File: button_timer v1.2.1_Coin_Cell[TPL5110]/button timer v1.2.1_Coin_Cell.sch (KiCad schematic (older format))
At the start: 24 parts, among them J1 Conn_01x05_Female, SW1 SW_Push, SW2 SW_Push, U1 TPS61097A, U3 TPL5111, X1 ESP-12E

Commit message: :rocket: :full_moon_with_face:
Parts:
- removed U3: TPL5111, handsolder:SOT-23-6handsoldering, symbol button-timer-v1.2.1_Coin_Cell-rescue:TPL5111-Timer-button-timer-rescue-button-t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
- added Q1: TSM2323, Package_TO_SOT_SMD:SOT-23, symbol Transistor_FET:TSM2301ACX
- added U2: TPL5110, Package_TO_SOT_SMD:SOT-23-6, symbol Timer:TPL5110
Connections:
- net GND: now also U2.2 (GND), U2.6 (EN/ONE_SHOT)
- net GPIO4: now also U2.4 (DONE)
- net at BT1.1 (+), C1.2, C5.2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: now also Q1.2 (S), U2.1 (VDD); no longer L1.1, U1.1 (VIN)
- net at R6.2, R8.2, SW1.2: now also U2.3 (DELAY/M_DRV)
- net at R7.1: now also U1.3 (EN)
- net at R7.2: now also L1.1, U1.1 (VIN), Q1.3 (D); no longer U1.3 (EN)
- new net: Q1.1 (G), U2.5 (DRV)
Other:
- moved on the sheet: C3, L1, R7, U1
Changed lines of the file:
@@
 Wire Wire Line
 	1300 5750 1300 5650
-$Comp
-L button-timer-v1.2.1_Coin_Cell-rescue:TPL5111-Timer-button-timer-rescue-button-timer-v1.2-rescue-button-timer-v1.2-rescue U3
-U 1 1 6031B6A7
-P 2250 5650
-F 0 "U3" H 2200 6331 50  0000 C CNN
-F 1 "TPL5111" H 2200 6240 50  0000 C CNN
-F 2 "handsolder:SOT-23-6handsoldering" H 2250 5650 50  0001 C CNN
-F 3 "http://www.ti.com/lit/ds/symlink/tpl5111.pdf" H 600 5800 50  0001 C CNN
-	1    2250 5650
-	1    0    0    -1
-$EndComp
 Text Label 2250 6050 3    50   ~ 0
 GND
@@
 Wire Wire Line
 	2650 4150 2700 4150
-Wire Wire Line
-	2750 5550 3050 5550
 Text Label 1650 5550 2    50   ~ 0
 GND
@@
 	2250 4150 2550 4150
 Wire Wire Line
-	2900 4400 2900 4100
+	4050 4700 4050 4400
 Wire Wire Line
 	2200 4150 2200 4350
@@
 L button-timer-v1.2.1_Coin_Cell-rescue:R-Device-button-timer-rescue-button-timer-v1.2-rescue-button-timer-v1.2-rescue R7
 U 1 1 602F7A06
-P 3200 5550
-F 0 "R7" H 3270 5596 50  0000 L CNN
-F 1 "10k" H 3270 5505 50  0000 L CNN
-F 2 "handsolder:R_0805_2012handsoldermod" V 3130 5550 50  0001 C CNN
-F 3 "~" H 3200 5550 50  0001 C CNN
-	1    3200 5550
-	0    -1   -1   0
-$EndComp
-Wire Wire Line
-	2700 4100 2900 4100
+P 4500 5700
+F 0 "R7" H 4570 5746 50  0000 L CNN
+F 1 "10k" H 4570 5655 50  0000 L CNN
+F 2 "handsolder:R_0805_2012handsoldermod" V 4430 5700 50  0001 C CNN
+F 3 "~" H 4500 5700 50  0001 C CNN
+	1    4500 5700
+	-1   0    0    1
+$EndComp
 Text Label 1500 5950 3    50   ~ 0
 GND
@@
 Wire Wire Line
 	1300 5650 1200 5650
-Connection ~ 2900 4100
-Wire Wire Line
-	4450 4300 4450 5550
-Wire Wire Line
-	2900 4100 3450 4100
-Wire Wire Line
-	3400 4650 3950 4650
-Wire Wire Line
-	3400 4650 3400 4400
-Wire Wire Line
-	3500 4200 3500 4300
-Wire Wire Line
-	3500 4300 3600 4300
-Connection ~ 4650 4450
-Wire Wire Line
-	4300 4450 4650 4450
-Wire Wire Line
-	4450 4300 4300 4300
+Connection ~ 4050 4400
+Wire Wire Line
+	5600 4600 5600 5850
+Wire Wire Line
+	4050 4400 4600 4400
+Wire Wire Line
+	4550 4950 5100 4950
+Wire Wire Line
+	4550 4950 4550 4700
+Wire Wire Line
+	4650 4500 4650 4600
+Wire Wire Line
+	4650 4600 4750 4600
+Connection ~ 5800 4750
+Wire Wire Line
+	5450 4750 5800 4750
+Wire Wire Line
+	5600 4600 5450 4600
 $Comp
 L button-timer-v1.2.1_Coin_Cell-rescue:TPS61097A-TPS-button-timer-v1.2-rescue U1
 U 1 1 6033543B
-P 3900 4150
-F 0 "U1" H 3950 4265 50  0000 C CNN
-F 1 "TPS61097A" H 3950 4174 50  0000 C CNN
-F 2 "handsolder:SOT-23-5_HandSolderingmod" H 4250 4100 50  0001 C CNN
-F 3 "" H 4250 4100 50  0001 C CNN
-	1    3900 4150
+P 5050 4450
+F 0 "U1" H 5100 4565 50  0000 C CNN
+F 1 "TPS61097A" H 5100 4474 50  0000 C CNN
+F 2 "handsolder:SOT-23-5_HandSolderingmod" H 5400 4400 50  0001 C CNN
+F 3 "" H 5400 4400 50  0001 C CNN
+	1    5050 4450
 	1    0    0    -1
 $EndComp
@@
 Text Label 6700 3600 0    50   ~ 0
 GPIO15
-Text Label 4700 4400 0    50   ~ 0
-VCC
-Text Label 4650 4750 0    50   ~ 0
-GND
-Wire Wire Line
-	4650 4450 4700 4450
+Text Label 5850 4700 0    50   ~ 0
+VCC
+Text Label 5800 5050 0    50   ~ 0
+GND
+Wire Wire Line
+	5800 4750 5850 4750
 $Comp
 L button-timer-v1.2.1_Coin_Cell-rescue:C-Device-button-timer-rescue-button-timer-v1.2-rescue-button-timer-v1.2-rescue C3
 U 1 1 602E3D4A
-P 4650 4600
-F 0 "C3" H 4765 4646 50  0000 L CNN
-F 1 "10uF" H 4765 4555 50  0000 L CNN
-F 2 "handsolder:C_0805_2012handsodermod" H 4688 4450 50  0001 C CNN
-F 3 "~" H 4650 4600 50  0001 C CNN
-	1    4650 4600
-	1    0    0    -1
-$EndComp
-Wire Wire Line
-	4700 4450 4700 4400
+P 5800 4900
+F 0 "C3" H 5915 4946 50  0000 L CNN
+F 1 "10uF" H 5915 4855 50  0000 L CNN
+F 2 "handsolder:C_0805_2012handsodermod" H 5838 4750 50  0001 C CNN
+F 3 "~" H 5800 4900 50  0001 C CNN
+	1    5800 4900
+	1    0    0    -1
+$EndComp
+Wire Wire Line
+	5850 4750 5850 4700
 $Comp
 L button-timer-v1.2.1_Coin_Cell-rescue:INDUCTOR-pspice-button-timer-rescue-button-timer-v1.2-rescue-button-timer-v1.2-rescue L1
 U 1 1 602E234D
-P 3150 4400
-F 0 "L1" H 3150 4615 50  0000 C CNN
-F 1 "4.7 uH" H 3150 4524 50  0000 C CNN
-F 2 "handsolder:SMD-1210_Pol_inductor" H 3150 4400 50  0001 C CNN
-F 3 "~" H 3150 4400 50  0001 C CNN
-	1    3150 4400
-	1    0    0    -1
-$EndComp
-Text Label 3600 4450 2    50   ~ 0
-GND
-Wire Wire Line
-	3450 4200 3500 4200
-Wire Wire Line
-	3450 4100 3450 4200
+P 4300 4700
+F 0 "L1" H 4300 4915 50  0000 C CNN
+F 1 "4.7 uH" H 4300 4824 50  0000 C CNN
+F 2 "handsolder:SMD-1210_Pol_inductor" H 4300 4700 50  0001 C CNN
+F 3 "~" H 4300 4700 50  0001 C CNN
+	1    4300 4700
+	1    0    0    -1
+$EndComp
+Text Label 4750 4750 2    50   ~ 0
+GND
+Wire Wire Line
+	4600 4500 4650 4500
+Wire Wire Line
+	4600 4400 4600 4500
 Text Label 6700 3100 0    50   ~ 0
 RX
@@
 $EndComp
 Wire Wire Line
-	3350 5550 4450 5550
+	4500 5850 5600 5850
 Wire Wire Line
 	2750 5650 3050 5650
@@
 Text Label 2850 4950 0    50   ~ 0
 GND
+$Comp
+L Timer:TPL5110 U2
+U 1 1 60350B91
+P 2250 5550
+F 0 "U2" H 2200 6131 50  0000 C CNN
+F 1 "TPL5110" H 2200 6040 50  0000 C CNN
+F 2 "Package_TO_SOT_SMD:SOT-23-6" H 2250 5550 50  0001 C CNN
+F 3 "http://www.ti.com/lit/ds/symlink/tpl5110.pdf" H 2050 5150 50  0001 C CNN
+	1    2250 5550
+	1    0    0    -1
+$EndComp
+Wire Wire Line
+	4500 5550 4500 4800
+Wire Wire Line
+	4500 4800 3950 4800
+Wire Wire Line
+	3950 4800 3950 4400
+Connection ~ 3950 4400
+Wire Wire Line
+	3950 4400 4050 4400
+Wire Wire Line
+	3350 5550 3350 4600
+Wire Wire Line
+	2750 5550 3350 5550
+$Comp
+L Transistor_FET:TSM2301ACX Q1
+U 1 1 6035BA2A
+P 3350 4400
+F 0 "Q1" V 3692 4400 50  0000 C CNN
+F 1 " TSM2323 " V 3601 4400 50  0000 C CNN
+F 2 "Package_TO_SOT_SMD:SOT-23" H 3550 4325 50  0001 L CIN
+F 3 "https://www.taiwansemi.com/products/datasheet/TSM2301A_C15.pdf" H 3350 4400 50  0001 L CNN
+	1    3350 4400
+	0    1    -1   0
+$EndComp
+Wire Wire Line
+	3550 4400 3550 4300
+Wire Wire Line
+	3550 4400 3950 4400
+Wire Wire Line
+	3150 4250 2750 4250
+Wire Wire Line
+	2750 4250 2750 4100
+Wire Wire Line
+	2750 4100 2700 4100
+Wire Wire Line
+	3150 4250 3150 4300
 $EndSCHEMATC

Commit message: 3D Models etwas verbessert
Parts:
- J1: footprint Connector_PinHeader_2.54mm:PinHeader_1x05_P2.54mm_Vertical -> handsolder:PinSocket_1x05_P2.54mm_Vertical_mod
- SW1: footprint Button_Switch_THT:SW_PUSH_6mm -> handsolder:SW_PUSH_6mm_H8mm_mod
- SW2: footprint Button_Switch_SMD:SW_SPST_EVQPE1 -> handsolder:SW_SPST_B3U-1000P_mod
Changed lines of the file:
@@
 F 0 "SW1" H 1200 5735 50  0000 C CNN
 F 1 "SW_Push" H 1200 5644 50  0000 C CNN
-F 2 "Button_Switch_THT:SW_PUSH_6mm" H 1200 5650 50  0001 C CNN
+F 2 "handsolder:SW_PUSH_6mm_H8mm_mod" H 1200 5650 50  0001 C CNN
 F 3 "~" H 1200 5650 50  0001 C CNN
 	1    1200 5450
@@
 F 0 "J1" H 8328 3576 50  0000 L CNN
 F 1 "Conn_01x05_Female" H 8328 3485 50  0000 L CNN
-F 2 "Connector_PinHeader_2.54mm:PinHeader_1x05_P2.54mm_Vertical" H 8300 3550 50  0001 C CNN
+F 2 "handsolder:PinSocket_1x05_P2.54mm_Vertical_mod" H 8300 3550 50  0001 C CNN
 F 3 "~" H 8300 3550 50  0001 C CNN
 	1    8300 3550
@@
 F 0 "SW2" H 7800 2335 50  0000 C CNN
 F 1 "SW_Push" H 7800 2244 50  0000 C CNN
-F 2 "Button_Switch_SMD:SW_SPST_EVQPE1" H 7800 2250 50  0001 C CNN
+F 2 "handsolder:SW_SPST_B3U-1000P_mod" H 7800 2250 50  0001 C CNN
 F 3 "~" H 7800 2250 50  0001 C CNN
 	1    7800 2050

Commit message: .
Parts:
- added C6: T495B476K006ATE450, CAPPM3528X210N, symbol SamacSys_Parts:T495B476K006ATE450
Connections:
- net GND: now also C6.2
- net VCC: now also C6.1
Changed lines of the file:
@@
 Wire Wire Line
 	3150 4250 3150 4300
+$Comp
+L SamacSys_Parts:T495B476K006ATE450 C6
+U 1 1 60365D39
+P 5300 3700
+F 0 "C6" V 5504 3830 50  0000 L CNN
+F 1 "T495B476K006ATE450" V 5595 3830 50  0000 L CNN
+F 2 "CAPPM3528X210N" H 5650 3750 50  0001 L CNN
+F 3 "https://connect.kemet.com:7667/gateway/IntelliData-ComponentDocumentation/1.0/download/specsheet/T495B476K006ATE450" H 5650 3650 50  0001 L CNN
+F 4 "Cap Tant Solid 47uF 6.3V B CASE 10% (3.5 X 2.8 X 1.9mm) SMD 3528-21 0.45 Ohm 125C Automotive T/R" H 5650 3550 50  0001 L CNN "Description"
+F 5 "2.1" H 5650 3450 50  0001 L CNN "Height"
+F 6 "Kemet" H 5650 3350 50  0001 L CNN "Manufacturer_Name"
+F 7 "T495B476K006ATE450" H 5650 3250 50  0001 L CNN "Manufacturer_Part_Number"
+F 8 "80-T495B476K6ATE450" H 5650 3150 50  0001 L CNN "Mouser Part Number"
+F 9 "https://www.mouser.com/Search/Refine.aspx?Keyword=80-T495B476K6ATE450" H 5650 3050 50  0001 L CNN "Mouser Price/Stock"
+F 10 "T495B476K006ATE450" H 5650 2950 50  0001 L CNN "Arrow Part Number"
+F 11 "https://www.arrow.com/en/products/t495b476k006ate450/kemet-corporation" H 5650 2850 50  0001 L CNN "Arrow Price/Stock"
+	1    5300 3700
+	0    1    1    0
+$EndComp
+Text Label 5300 4200 0    50   ~ 0
+GND
 $EndSCHEMATC

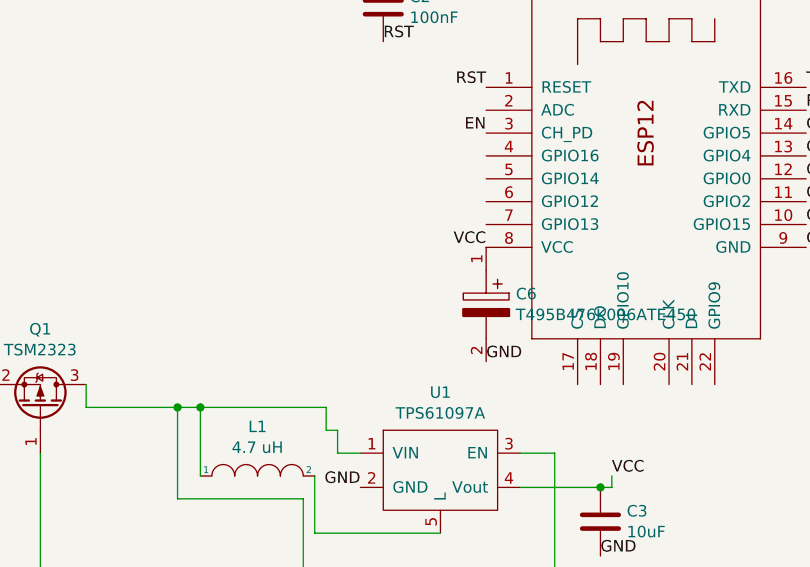
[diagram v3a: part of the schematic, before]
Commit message: Added 100nF decoupling capacitors between VCC and Ground of the ESP
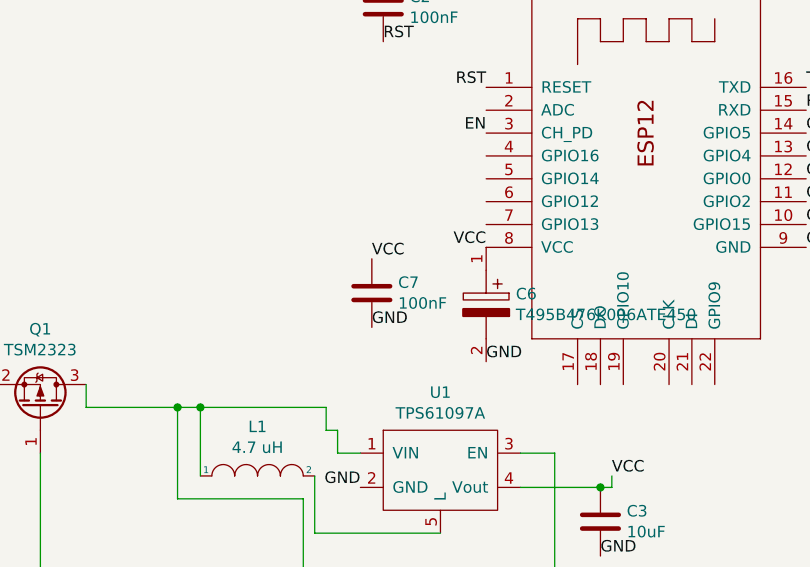
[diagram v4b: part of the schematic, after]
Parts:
- added C7: 100nF, handsolder:C_0402_1005Metric_Pad0.74x0.62mm_HandSoldermod, symbol Device:C
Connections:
- net GND: now also C7.2
- net VCC: now also C7.1
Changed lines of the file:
@@
 Text Label 5300 4200 0    50   ~ 0
 GND
+$Comp
+L Device:C C7
+U 1 1 60368125
+P 4800 3900
+F 0 "C7" H 4915 3946 50  0000 L CNN
+F 1 "100nF" H 4915 3855 50  0000 L CNN
+F 2 "handsolder:C_0402_1005Metric_Pad0.74x0.62mm_HandSoldermod" H 4838 3750 50  0001 C CNN
+F 3 "~" H 4800 3900 50  0001 C CNN
+	1    4800 3900
+	1    0    0    -1
+$EndComp
+Text Label 4800 3750 0    50   ~ 0
+VCC
+Text Label 4800 4050 0    50   ~ 0
+GND
 $EndSCHEMATC

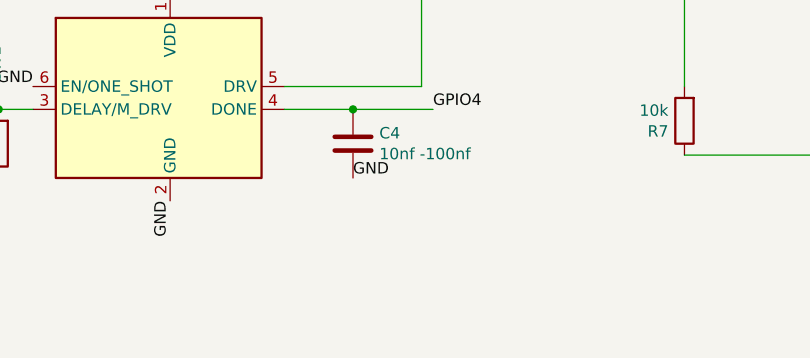
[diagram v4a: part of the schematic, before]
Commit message: turned around some of the LIPO connectors
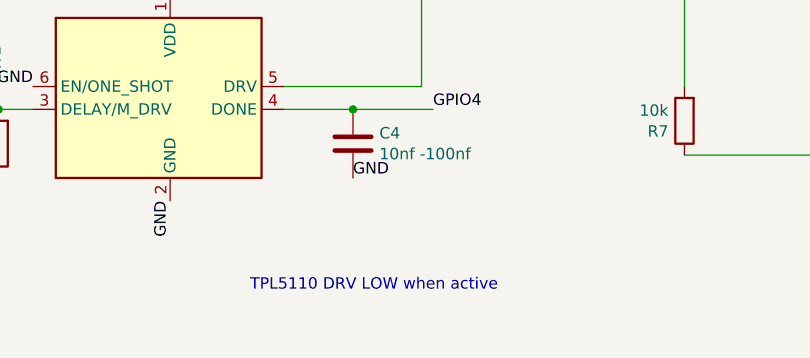
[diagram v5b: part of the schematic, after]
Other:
- note added: "TPL5110 DRV LOW when active"
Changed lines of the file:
@@
 Text Label 4800 4050 0    50   ~ 0
 GND
+Text Notes 2600 6450 0    50   ~ 0
+TPL5110 DRV LOW when active
 $EndSCHEMATC
